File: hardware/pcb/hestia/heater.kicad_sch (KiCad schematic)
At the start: 22 parts

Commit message: Fix some ERC violations
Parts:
- C5, C6, C7: value (none) -> 22uF 16V; footprint (none) -> Capacitor_SMD:C_1206_3216Metric
- C57: value (none) -> 0.1uF; footprint (none) -> Capacitor_SMD:C_0603_1608Metric_Pad1.08x0.95mm_HandSolder
- D5: value (none) -> ORANGE LED; footprint (none) -> LED_SMD:LED_0805_2012Metric_Pad1.15x1.40mm_HandSolder
- D7: value (none) -> BAT54S; footprint (none) -> Package_TO_SOT_SMD:SOT-23
- FB13: value (none) -> MMZ1608A222BTA00; footprint (none) -> Resistor_SMD:R_0603_1608Metric_Pad0.98x0.95mm_HandSolder
- Q1: value (none) -> FDS8876; footprint (none) -> Package_SO:SOIC-8_3.9x4.9mm_P1.27mm
- R17, R18, R19, R25, R44: value (none) -> 10K; footprint (none) -> Resistor_SMD:R_0603_1608Metric_Pad0.98x0.95mm_HandSolder
- R2: value (none) -> 470R; footprint (none) -> Resistor_SMD:R_0603_1608Metric_Pad0.98x0.95mm_HandSolder
- R26: value (none) -> Heater; footprint (none) -> NetTie:NetTie-2_SMD_Pad0.5mm
- R3: value (none) -> 47K; footprint (none) -> Resistor_SMD:R_0603_1608Metric_Pad0.98x0.95mm_HandSolder
- R41: value (none) -> 100R; footprint (none) -> Resistor_SMD:R_0603_1608Metric_Pad0.98x0.95mm_HandSolder
- R42: value (none) -> 499R; footprint (none) -> Capacitor_SMD:C_0402_1005Metric
- R43: value (none) -> LVK12R010CER; footprint (none) -> Hestia:LVK12R010CER
- SW2: value (none) -> SW_Push_Open; footprint (none) -> Connector_PinHeader_2.54mm:PinHeader_1x02_P2.54mm_Vertical
- TP1: value (none) -> TestPoint; footprint (none) -> TestPoint:TestPoint_Pad_2.0x2.0mm
- U10: value (none) -> INA826; footprint (none) -> Package_SON:WSON-8-1EP_3x3mm_P0.5mm_EP1.2x2mm
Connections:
- net +3V3 renamed +3.3V

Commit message: Remove some silkscreen refs
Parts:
- SW2: now left out of the parts list
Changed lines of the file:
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@@
   )
   (symbol (lib_id "Switch:SW_Push_Open") (at 129.54 78.74 90) (unit 1)
-    (in_bom yes) (on_board yes) (fields_autoplaced)
+    (in_bom no) (on_board yes) (fields_autoplaced)
     (property "Reference" "SW2" (id 0) (at 130.81 77.4699 90)
       (effects (font (size 1.27 1.27)) (justify right))

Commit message: changed all 10K to 0.5% to be same component. changed led part numbers back to 0805. - my mistake. i had thought the footprints had changed to 0603. filled in other missing digikey part numbers. added manufacturer names and manufacturer part numbers. finished adding SMD/TH entry for component types. Excluded R4/R5 DNP part numbers from BOM
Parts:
- C5, C6, C7: value 22uF 16V -> (none); footprint Capacitor_SMD:C_1206_3216Metric -> (none); Manufacturer (none) -> Samsung Electro-Mechanics; Mfr PN (none) -> CL31A226MOCLNNC; Type (none) -> SMD
- C57: value 0.1uF -> (none); footprint Capacitor_SMD:C_0603_1608Metric_Pad1.08x0.95mm_HandSolder -> (none); Manufacturer (none) -> Samsung Electro-Mechanics; Mfr PN (none) -> CL10B104KB8WPND; Type (none) -> SMD
- D5: value ORANGE LED -> (none); footprint LED_SMD:LED_0805_2012Metric_Pad1.15x1.40mm_HandSolder -> (none); Digikey Part 475-2486-1-ND -> 475-2488-1-ND; Manufacturer (none) -> OSRAM Opto (ams OSRAM); Mfr PN (none) -> LO R976-PS-1; Type (none) -> SMD
- D7: value BAT54S -> (none); footprint Package_TO_SOT_SMD:SOT-23 -> (none); Manufacturer (none) -> onsemi; Mfr PN (none) -> BAT54SWT1G; Type (none) -> SMD
- FB13: value MMZ1608A222BTA00 -> (none); footprint Resistor_SMD:R_0603_1608Metric_Pad0.98x0.95mm_HandSolder -> (none); Manufacturer (none) -> TDK; Mfr PN (none) -> MMZ1608A222BTA00; Type (none) -> SMD
- Q1: value FDS8876 -> (none); footprint Package_SO:SOIC-8_3.9x4.9mm_P1.27mm -> (none); Manufacturer (none) -> onsemi; Mfr PN (none) -> FDS8876; Type (none) -> SMD
- R17, R18, R19, R25, R44: value 10K -> (none); footprint Resistor_SMD:R_0603_1608Metric_Pad0.98x0.95mm_HandSolder -> (none); Digikey Part (none) -> RR08P10.0KDCT-ND; Manufacturer (none) -> Susumu; Mfr PN (none) -> RR0816P-103-D; Type (none) -> SMD
- R2: value 470R -> (none); footprint Resistor_SMD:R_0603_1608Metric_Pad0.98x0.95mm_HandSolder -> (none); Manufacturer (none) -> Rohm Semiconductor; Mfr PN (none) -> ESR03EZPF4700; Type (none) -> SMD
- R26: value Heater -> (none); footprint NetTie:NetTie-2_SMD_Pad0.5mm -> (none)
- R3: value 47K -> (none); footprint Resistor_SMD:R_0603_1608Metric_Pad0.98x0.95mm_HandSolder -> (none); Manufacturer (none) -> Panasonic Electronic Components; Mfr PN (none) -> ERJ-PA3J473V; Type (none) -> SMD
- R41: value 100R -> (none); footprint Resistor_SMD:R_0603_1608Metric_Pad0.98x0.95mm_HandSolder -> (none); Digikey Part (none) -> 13-RC0603JR-13100RLCT-ND; Manufacturer (none) -> YAGEO; Mfr PN (none) -> RC0603JR-13100RL; Type (none) -> SMD
- R42: value 499R -> (none); footprint Capacitor_SMD:C_0402_1005Metric -> (none); Digikey Part (none) -> P499DCCT-ND; Manufacturer (none) -> Panasonic Electronic Components; Mfr PN (none) -> ERA-2AEB4990X; Type (none) -> SMD
- R43: value LVK12R010CER -> (none); footprint Hestia:LVK12R010CER -> (none); Manufacturer (none) -> Ohmite; Mfr PN (none) -> LVK12R010CER; Type (none) -> SMD
- SW2: value SW_Push_Open -> (none); footprint Connector_PinHeader_2.54mm:PinHeader_1x02_P2.54mm_Vertical -> (none)
- TP1: value TestPoint -> (none); footprint TestPoint:TestPoint_Pad_2.0x2.0mm -> (none)
- U10: value INA826 -> (none); footprint Package_SON:WSON-8-1EP_3x3mm_P0.5mm_EP1.2x2mm -> (none); Manufacturer (none) -> Texas Instruments; Mfr PN (none) -> INA826AIDRGR; Type (none) -> SMD

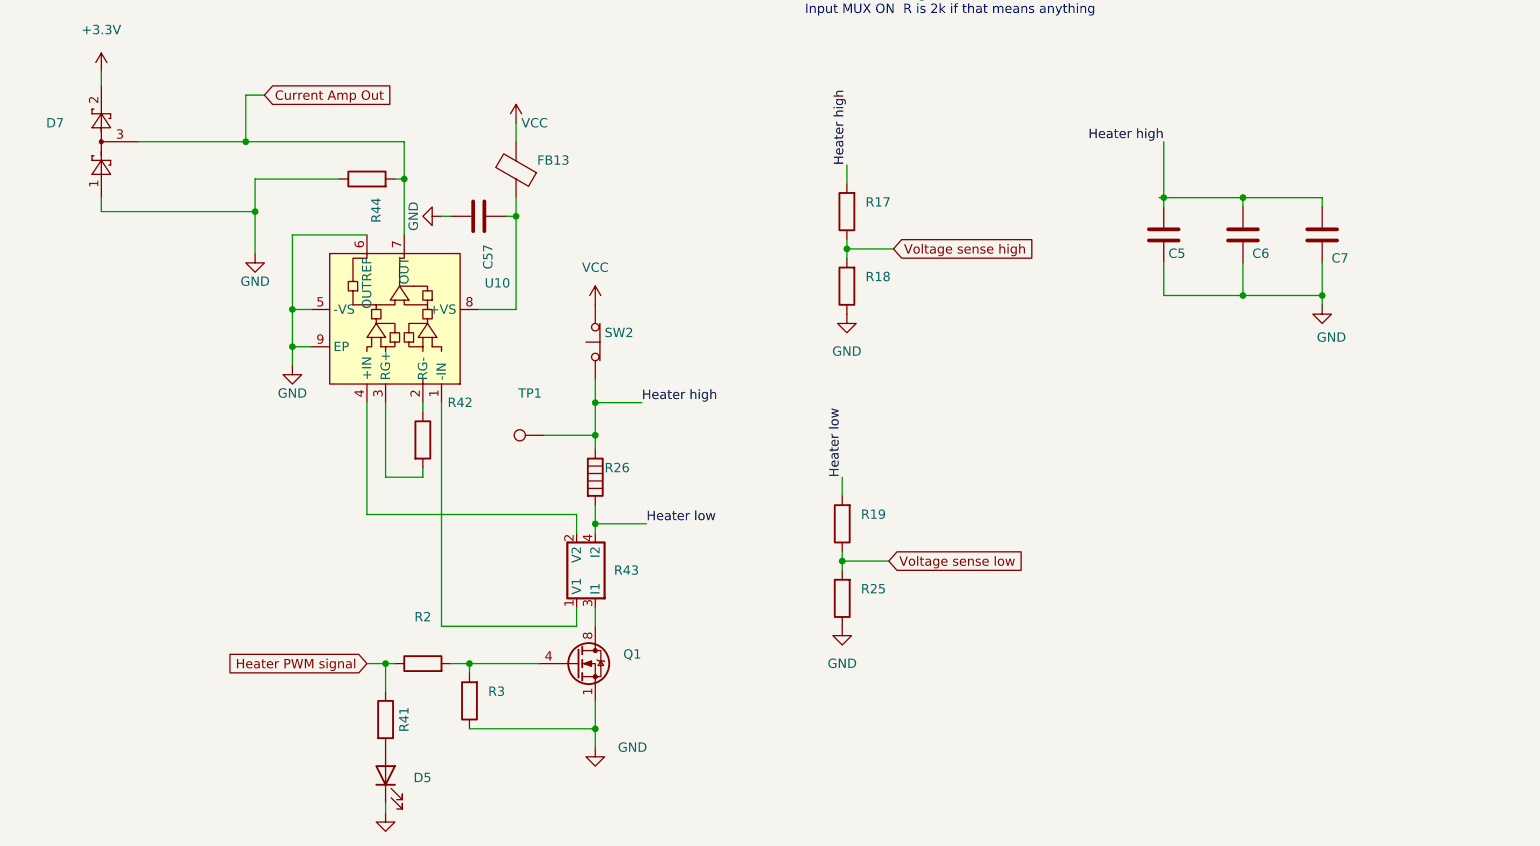
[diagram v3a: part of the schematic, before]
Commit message: c39 digikey and mfr part numbers changed to a 100pf part number. It had previously erroneously been given a 10pf part number
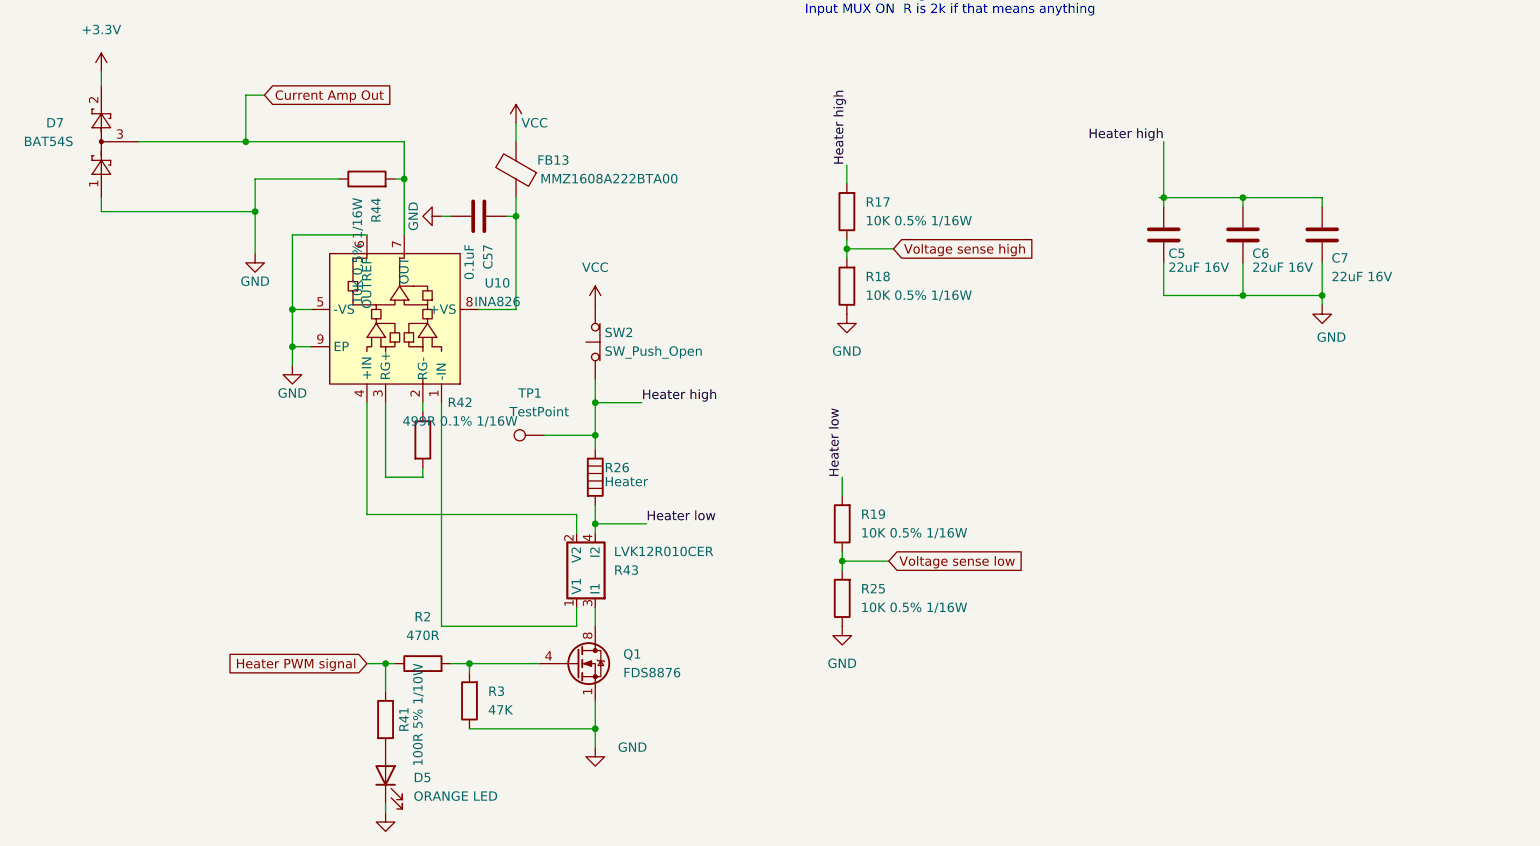
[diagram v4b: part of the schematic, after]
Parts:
- C5, C6, C7: value (none) -> 22uF 16V
- C57: value (none) -> 0.1uF
- D5: value (none) -> ORANGE LED
- D7: value (none) -> BAT54S
- FB13: value (none) -> MMZ1608A222BTA00
- Q1: value (none) -> FDS8876
- R17, R18, R19, R25, R44: value (none) -> 10K 0.5% 1/16W
- R2: value (none) -> 470R
- R26: value (none) -> Heater
- R3: value (none) -> 47K
- R41: value (none) -> 100R 5% 1/10W
- R42: value (none) -> 499R 0.1% 1/16W
- R43: value (none) -> LVK12R010CER
- SW2: value (none) -> SW_Push_Open
- TP1: value (none) -> TestPoint
- U10: value (none) -> INA826
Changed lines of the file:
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@@
       (effects (font (size 1.27 1.27)) (justify left))
     )
-    (property "Value" "" (id 1) (at 130.81 97.79 0)
+    (property "Value" "Heater" (id 1) (at 130.81 97.79 0)
       (effects (font (size 1.27 1.27)) (justify left))
     )
@@
     (in_bom yes) (on_board yes) (fields_autoplaced)
     (property "Reference" "U10" (id 0) (at 116.205 70.7136 90))
-    (property "Value" "" (id 1) (at 116.205 73.2536 90))
+    (property "Value" "INA826" (id 1) (at 116.205 73.2536 90))
     (property "Footprint" "" (id 2) (at 103.505 76.835 0)
       (effects (font (size 1.27 1.27)) hide)
@@
     (in_bom yes) (on_board yes) (fields_autoplaced)
     (property "Reference" "R2" (id 0) (at 106.045 116.205 90))
-    (property "Value" "" (id 1) (at 106.045 118.745 90))
+    (property "Value" "470R" (id 1) (at 106.045 118.745 90))
     (property "Footprint" "" (id 2) (at 106.045 124.333 90)
       (effects (font (size 1.27 1.27)) hide)
@@
       (effects (font (size 1.27 1.27)) (justify right))
     )
-    (property "Value" "" (id 1) (at 104.775 140.6524 90)
+    (property "Value" "ORANGE LED" (id 1) (at 104.775 140.6524 90)
       (effects (font (size 1.27 1.27)) (justify right))
     )
@@
       (effects (font (size 1.27 1.27)) (justify left))
     )
-    (property "Value" "" (id 1) (at 112.3951 65.405 0)
+    (property "Value" "0.1uF" (id 1) (at 112.3951 65.405 0)
       (effects (font (size 1.27 1.27)) (justify left))
     )
@@
       (effects (font (size 1.27 1.27)) (justify right))
     )
-    (property "Value" "" (id 1) (at 130.81 80.0099 90)
+    (property "Value" "SW_Push_Open" (id 1) (at 130.81 80.0099 90)
       (effects (font (size 1.27 1.27)) (justify right))
     )
@@
       (effects (font (size 1.27 1.27)) (justify right))
     )
-    (property "Value" "" (id 1) (at 165.735 104.7749 0)
+    (property "Value" "10K 0.5% 1/16W" (id 1) (at 165.735 104.7749 0)
       (effects (font (size 1.27 1.27)) (justify right))
     )
@@
       (effects (font (size 1.27 1.27)) (justify right))
     )
-    (property "Value" "" (id 1) (at 166.37 72.3899 0)
+    (property "Value" "10K 0.5% 1/16W" (id 1) (at 166.37 72.3899 0)
       (effects (font (size 1.27 1.27)) (justify right))
     )
@@
       (effects (font (size 1.27 1.27)) (justify right))
     )
-    (property "Value" "" (id 1) (at 165.735 114.9349 0)
+    (property "Value" "10K 0.5% 1/16W" (id 1) (at 165.735 114.9349 0)
       (effects (font (size 1.27 1.27)) (justify right))
     )
@@
       (effects (font (size 1.27 1.27)) (justify left))
     )
-    (property "Value" "" (id 1) (at 58.42 51.435 90)
+    (property "Value" "BAT54S" (id 1) (at 58.42 51.435 90)
       (effects (font (size 1.27 1.27)) (justify left))
     )
@@
     (in_bom yes) (on_board yes)
     (property "Reference" "R42" (id 0) (at 111.125 86.995 0))
-    (property "Value" "" (id 1) (at 111.125 89.535 0))
+    (property "Value" "499R 0.1% 1/16W" (id 1) (at 111.125 89.535 0))
     (property "Footprint" "" (id 2) (at 104.267 92.075 90)
       (effects (font (size 1.27 1.27)) hide)
@@
     (in_bom yes) (on_board yes)
     (property "Reference" "TP1" (id 0) (at 120.65 85.725 90))
-    (property "Value" "" (id 1) (at 121.92 88.265 90))
+    (property "Value" "TestPoint" (id 1) (at 121.92 88.265 90))
     (property "Footprint" "" (id 2) (at 122.555 86.36 0)
       (effects (font (size 1.27 1.27)) hide)
@@
       (effects (font (size 1.27 1.27)) (justify right))
     )
-    (property "Value" "" (id 1) (at 97.1551 59.055 0)
+    (property "Value" "10K 0.5% 1/16W" (id 1) (at 97.1551 59.055 0)
       (effects (font (size 1.27 1.27)) (justify right))
     )
@@
       (effects (font (size 1.27 1.27)) (justify right))
     )
-    (property "Value" "" (id 1) (at 132.08 107.315 0)
+    (property "Value" "LVK12R010CER" (id 1) (at 132.08 107.315 0)
       (effects (font (size 1.27 1.27)) (justify right))
     )
@@
       (effects (font (size 1.27 1.27)) (justify right))
     )
-    (property "Value" "" (id 1) (at 166.37 62.2299 0)
+    (property "Value" "10K 0.5% 1/16W" (id 1) (at 166.37 62.2299 0)
       (effects (font (size 1.27 1.27)) (justify right))
     )
@@
       (effects (font (size 1.27 1.27)) (justify left))
     )
-    (property "Value" "" (id 1) (at 219.075 68.58 0)
+    (property "Value" "22uF 16V" (id 1) (at 219.075 68.58 0)
       (effects (font (size 1.27 1.27)) (justify left))
     )
@@
     (in_bom yes) (on_board yes)
     (property "Reference" "R41" (id 0) (at 103.505 130.175 90))
-    (property "Value" "" (id 1) (at 105.41 129.54 90))
+    (property "Value" "100R 5% 1/10W" (id 1) (at 105.41 129.54 90))
     (property "Footprint" "" (id 2) (at 99.187 130.175 90)
       (effects (font (size 1.27 1.27)) hide)
@@
       (effects (font (size 1.27 1.27)) (justify left))
     )
-    (property "Value" "" (id 1) (at 207.645 68.58 0)
+    (property "Value" "22uF 16V" (id 1) (at 207.645 68.58 0)
       (effects (font (size 1.27 1.27)) (justify left))
     )
@@
       (effects (font (size 1.27 1.27)) (justify left))
     )
-    (property "Value" "" (id 1) (at 229.87 69.85 0)
+    (property "Value" "22uF 16V" (id 1) (at 229.87 69.85 0)
       (effects (font (size 1.27 1.27)) (justify left))
     )
@@
       (effects (font (size 1.27 1.27)) (justify left))
     )
-    (property "Value" "" (id 1) (at 133.35 123.8249 0)
+    (property "Value" "FDS8876" (id 1) (at 133.35 123.8249 0)
       (effects (font (size 1.27 1.27)) (justify left))
     )
@@
     (in_bom yes) (on_board yes)
     (property "Reference" "FB13" (id 0) (at 123.825 53.975 0))
-    (property "Value" "" (id 1) (at 131.445 56.515 0))
+    (property "Value" "MMZ1608A222BTA00" (id 1) (at 131.445 56.515 0))
     (property "Footprint" "" (id 2) (at 120.523 55.245 90)
       (effects (font (size 1.27 1.27)) hide)
@@
       (effects (font (size 1.27 1.27)) (justify right))
     )
-    (property "Value" "" (id 1) (at 114.935 128.9049 0)
-      (effects (font (size 1.27 1.27)) (justify right))
-    )
+    (property "Value" "47K" (id 1) (at 114.935 128.9049 0)
+      (effects (font (size 1.27 1.27)) (justify right))
+    )
